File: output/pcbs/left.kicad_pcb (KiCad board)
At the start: 2 copper layers, 130.3 x 118.5 mm, 47 parts

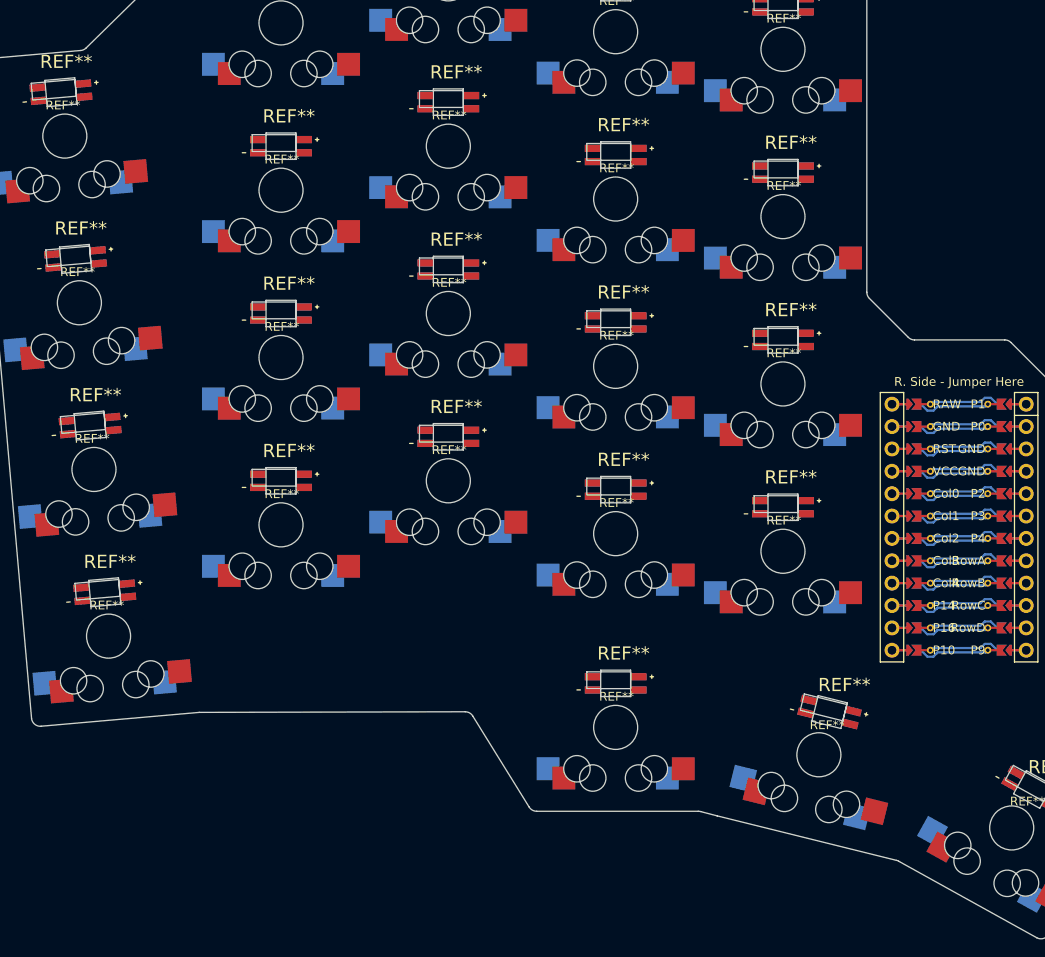
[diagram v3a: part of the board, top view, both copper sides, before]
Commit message: moving to seeed nrf52840 bc of rgb. footprint pretty much done
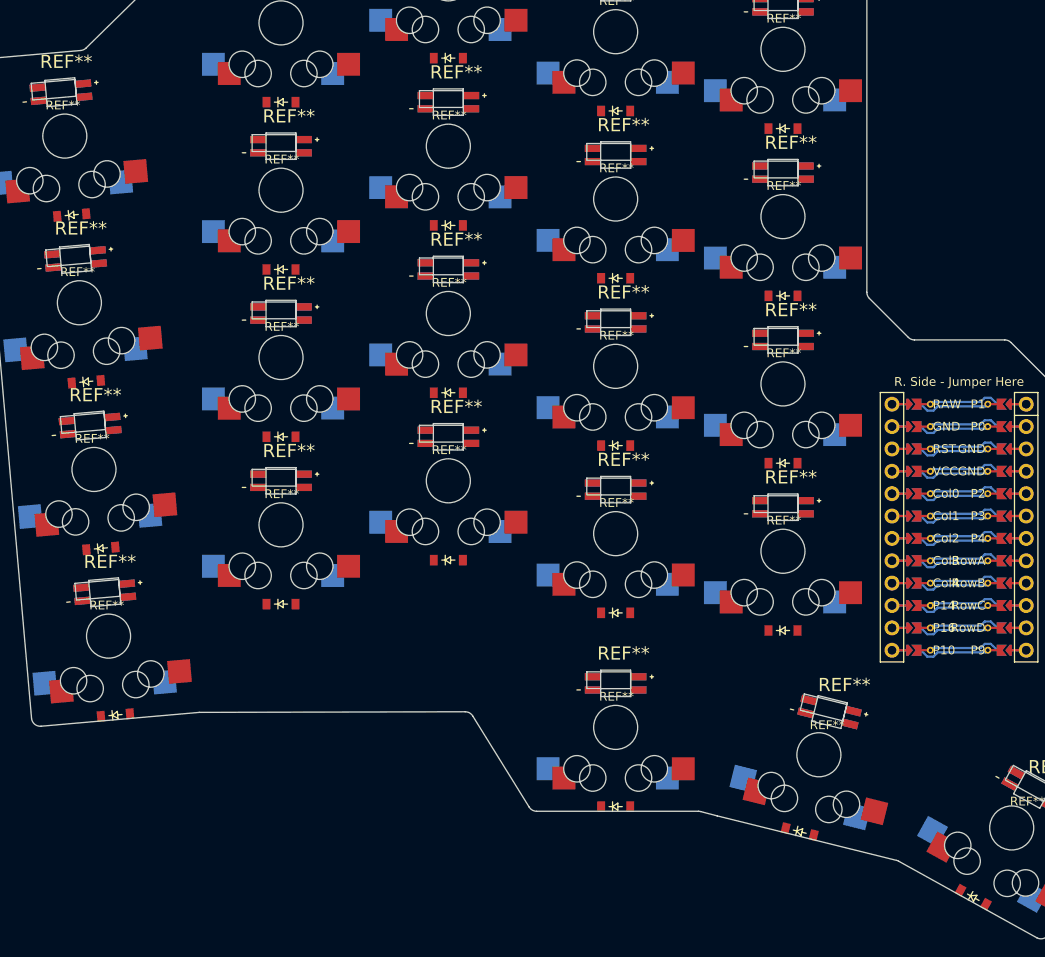
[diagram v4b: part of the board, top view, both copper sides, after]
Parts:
- added D1: , ComboDiode, F.Cu at (100.8, 109.0)
- added D10: , ComboDiode, F.Cu at (138.6, 72.4)
- added D11: , ComboDiode, F.Cu at (138.6, 53.4)
- added D12: , ComboDiode, F.Cu at (138.6, 34.4)
- added D13: , ComboDiode, F.Cu at (157.6, 97.4)
- added D14: , ComboDiode, F.Cu at (157.6, 78.4)
- added D15: , ComboDiode, F.Cu at (157.6, 59.4)
- added D16: , ComboDiode, F.Cu at (157.6, 40.4)
- added D17: , ComboDiode, F.Cu at (176.6, 99.4)
- added D18: , ComboDiode, F.Cu at (176.6, 80.4)
- added D19: , ComboDiode, F.Cu at (176.6, 61.4)
- added D2: , ComboDiode, F.Cu at (99.1, 90.0)
- added D20: , ComboDiode, F.Cu at (176.6, 42.4)
- added D21: , ComboDiode, F.Cu at (157.6, 119.4)
- added D22: , ComboDiode, F.Cu at (178.5, 122.2)
- added D23: , ComboDiode, F.Cu at (198.2, 129.7)
- added D3: , ComboDiode, F.Cu at (97.5, 71.1)
- added D4: , ComboDiode, F.Cu at (95.8, 52.2)
- added D5: , ComboDiode, F.Cu at (119.6, 96.4)
- added D6: , ComboDiode, F.Cu at (119.6, 77.4)
- added D7: , ComboDiode, F.Cu at (119.6, 58.4)
- added D8: , ComboDiode, F.Cu at (119.6, 39.4)
- added D9: , ComboDiode, F.Cu at (138.6, 91.4)

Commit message: starting to work on the ergogen side again
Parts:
- added 19.051: 74HC595, SOIC-16_3.9x9.9mm_P1.27mm, B.Cu at (0.00, 25.0)
- MCU1: footprint nice_nano -> xiao-ble
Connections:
- net MCU1_14 renamed VUSB
- net MCU1_17 renamed RST
- net MCU1_19 renamed BAT+
- net MCU1_6 renamed P5
- net MCU1_7 renamed P6
- net MCU1_8 renamed P7
- D1 pad 1: RowA -> Row0
- D10 pad 1: RowB -> Row1
- D11 pad 1: RowC -> Row2
- D12 pad 1: RowD -> Row3
- D13 pad 1: RowA -> Row0
- D14 pad 1: RowB -> Row1
- D15 pad 1: RowC -> Row2
- D16 pad 1: RowD -> Row3
- D17 pad 1: RowA -> Row0
- D18 pad 1: RowB -> Row1
- D19 pad 1: RowC -> Row2
- D2 pad 1: RowB -> Row1
- D20 pad 1: RowD -> Row3
- D21 pad 1: RowE -> Row4
- D22 pad 1: RowE -> Row4
- D23 pad 1: RowE -> Row4
- D3 pad 1: RowC -> Row2
- D4 pad 1: RowD -> Row3
- D5 pad 1: RowA -> Row0
- D6 pad 1: RowB -> Row1
- D7 pad 1: RowC -> Row2
- D8 pad 1: RowD -> Row3
- D9 pad 1: RowA -> Row0
- MCU1 pad 1: MCU1_1 -> Row0
- MCU1 pad 10: MCU1_10 -> RCLK
- MCU1 pad 11: MCU1_11 -> SER
- MCU1 pad 12: MCU1_12 -> VCC
- MCU1 pad 13: MCU1_13 -> GND
- MCU1 pad 2: MCU1_2 -> Row1
- MCU1 pad 3: MCU1_3 -> Row2
- MCU1 pad 4: MCU1_4 -> Row3
- MCU1 pad 5: MCU1_5 -> Row4
- MCU1 pad 9: MCU1_9 -> SRCLK
- REF** pad 1: Col4 -> Col2
- REF** pad 1: Col5 -> Col3
- REF** pad 1: Col5 -> Col4
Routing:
- net Col0: track 122.0 -> 0.00 mm
- net middle_home: track 121.7 -> 0.00 mm
- net inner_home: track 50.9 -> 0.00 mm
- net inner_top: track 50.9 -> 0.00 mm

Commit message: pushing to github
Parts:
- removed REF** (x23): k27, gateron-ks27-hotswap-reversible
- removed REF** (x23): LED_SK6812-E, LED_SK6812-E
- added LED1: , ceoloide:led_SK6812mini-e (per-keysingle-side), B.Cu at (98.9, 94.9)
- added LED10: , ceoloide:led_SK6812mini-e (per-keysingle-side), B.Cu at (138.0, 58.2)
- added LED11: , ceoloide:led_SK6812mini-e (per-keysingle-side), B.Cu at (138.0, 39.2)
- added LED12: , ceoloide:led_SK6812mini-e (per-keysingle-side), B.Cu at (138.0, 20.2)
- added LED13: , ceoloide:led_SK6812mini-e (per-keysingle-side), B.Cu at (157.0, 83.2)
- added LED14: , ceoloide:led_SK6812mini-e (per-keysingle-side), B.Cu at (157.0, 64.2)
- added LED15: , ceoloide:led_SK6812mini-e (per-keysingle-side), B.Cu at (157.0, 45.2)
- added LED16: , ceoloide:led_SK6812mini-e (per-keysingle-side), B.Cu at (157.0, 26.2)
- added LED17: , ceoloide:led_SK6812mini-e (per-keysingle-side), B.Cu at (176.0, 85.2)
- added LED18: , ceoloide:led_SK6812mini-e (per-keysingle-side), B.Cu at (176.0, 66.2)
- added LED19: , ceoloide:led_SK6812mini-e (per-keysingle-side), B.Cu at (176.0, 47.2)
- added LED2: , ceoloide:led_SK6812mini-e (per-keysingle-side), B.Cu at (97.3, 75.9)
- added LED20: , ceoloide:led_SK6812mini-e (per-keysingle-side), B.Cu at (176.0, 28.2)
- added LED21: , ceoloide:led_SK6812mini-e (per-keysingle-side), B.Cu at (157.0, 105.2)
- added LED22: , ceoloide:led_SK6812mini-e (per-keysingle-side), B.Cu at (181.3, 108.3)
- added LED23: , ceoloide:led_SK6812mini-e (per-keysingle-side), B.Cu at (204.6, 116.9)
- added LED3: , ceoloide:led_SK6812mini-e (per-keysingle-side), B.Cu at (95.6, 57.0)
- added LED4: , ceoloide:led_SK6812mini-e (per-keysingle-side), B.Cu at (94.0, 38.1)
- added LED5: , ceoloide:led_SK6812mini-e (per-keysingle-side), B.Cu at (119.0, 82.2)
- added LED6: , ceoloide:led_SK6812mini-e (per-keysingle-side), B.Cu at (119.0, 63.2)
- added LED7: , ceoloide:led_SK6812mini-e (per-keysingle-side), B.Cu at (119.0, 44.2)
- added LED8: , ceoloide:led_SK6812mini-e (per-keysingle-side), B.Cu at (119.0, 25.2)
- added LED9: , ceoloide:led_SK6812mini-e (per-keysingle-side), B.Cu at (138.0, 77.2)
- added S1: , ceoloide:switch_gateron_ks27_ks33, B.Cu at (100.0, 100.0)
- added S10: , ceoloide:switch_gateron_ks27_ks33, B.Cu at (138.6, 63.4)
- added S11: , ceoloide:switch_gateron_ks27_ks33, B.Cu at (138.6, 44.4)
- added S12: , ceoloide:switch_gateron_ks27_ks33, B.Cu at (138.6, 25.4)
- added S13: , ceoloide:switch_gateron_ks27_ks33, B.Cu at (157.6, 88.4)
- added S14: , ceoloide:switch_gateron_ks27_ks33, B.Cu at (157.6, 69.4)
- added S15: , ceoloide:switch_gateron_ks27_ks33, B.Cu at (157.6, 50.4)
- added S16: , ceoloide:switch_gateron_ks27_ks33, B.Cu at (157.6, 31.4)
- added S17: , ceoloide:switch_gateron_ks27_ks33, B.Cu at (176.6, 90.4)
- added S18: , ceoloide:switch_gateron_ks27_ks33, B.Cu at (176.6, 71.4)
- added S19: , ceoloide:switch_gateron_ks27_ks33, B.Cu at (176.6, 52.4)
- added S2: , ceoloide:switch_gateron_ks27_ks33, B.Cu at (98.3, 81.1)
- added S20: , ceoloide:switch_gateron_ks27_ks33, B.Cu at (176.6, 33.4)
- added S21: , ceoloide:switch_gateron_ks27_ks33, B.Cu at (157.6, 110.4)
- added S22: , ceoloide:switch_gateron_ks27_ks33, B.Cu at (180.7, 113.5)
- added S23: , ceoloide:switch_gateron_ks27_ks33, B.Cu at (202.6, 121.8)
- added S3: , ceoloide:switch_gateron_ks27_ks33, B.Cu at (96.7, 62.1)
- added S4: , ceoloide:switch_gateron_ks27_ks33, B.Cu at (95.0, 43.2)
- added S5: , ceoloide:switch_gateron_ks27_ks33, B.Cu at (119.6, 87.4)
- added S6: , ceoloide:switch_gateron_ks27_ks33, B.Cu at (119.6, 68.4)
- added S7: , ceoloide:switch_gateron_ks27_ks33, B.Cu at (119.6, 49.4)
- added S8: , ceoloide:switch_gateron_ks27_ks33, B.Cu at (119.6, 30.4)
- added S9: , ceoloide:switch_gateron_ks27_ks33, B.Cu at (138.6, 82.4)
- added _1: SOT65P210X110-5N, SOT65P210X110-5N, F.Cu at (0.00, 0.00)
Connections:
- MCU1 pad 6: P5 -> LED_3v3
